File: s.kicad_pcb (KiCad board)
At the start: 2 copper layers, 3 parts, among them J1 USB4085-GF-A_REVB, U1 ESP32-S3-WROOM-1, U2 MCP1825S

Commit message: add supporting stuff and assigned footprints
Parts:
- added C1: 1uF, Capacitor_SMD:C_0805_2012Metric_Pad1.18x1.45mm_HandSolder, F.Cu at (187.0, 114.8)
- added C2: 10uF, Capacitor_SMD:C_0805_2012Metric_Pad1.18x1.45mm_HandSolder, F.Cu at (187.0, 117.8)
- added C3: 1uF, Capacitor_SMD:C_0805_2012Metric_Pad1.18x1.45mm_HandSolder, F.Cu at (187.0, 120.8)
- added C4: 0.1uF, Capacitor_SMD:C_0805_2012Metric_Pad1.18x1.45mm_HandSolder, F.Cu at (187.0, 123.8)
- added C5: 0.1uF, Capacitor_SMD:C_0805_2012Metric_Pad1.18x1.45mm_HandSolder, F.Cu at (187.0, 126.8)
- added C6: 10uF, Capacitor_SMD:C_0805_2012Metric_Pad1.18x1.45mm_HandSolder, F.Cu at (187.0, 129.8)
- added D1: ~, Diode_SMD:D_SOD-323_HandSoldering, F.Cu at (243.7, 42.4)
- added D10: ~, Diode_SMD:D_SOD-323_HandSoldering, F.Cu at (248.8, 48.3)
- added D11: ~, Diode_SMD:D_SOD-323_HandSoldering, F.Cu at (248.8, 51.2)
- added D12: ~, Diode_SMD:D_SOD-323_HandSoldering, F.Cu at (248.8, 54.2)
- added D13: ~, Diode_SMD:D_SOD-323_HandSoldering, F.Cu at (248.8, 57.1)
- added D14: ~, Diode_SMD:D_SOD-323_HandSoldering, F.Cu at (248.8, 60.1)
- added D15: ~, Diode_SMD:D_SOD-323_HandSoldering, F.Cu at (253.8, 42.4)
- added D16: ~, Diode_SMD:D_SOD-323_HandSoldering, F.Cu at (253.8, 45.3)
- added D17: ~, Diode_SMD:D_SOD-323_HandSoldering, F.Cu at (253.8, 48.3)
- added D18: ~, Diode_SMD:D_SOD-323_HandSoldering, F.Cu at (253.8, 51.2)
- added D19: ~, Diode_SMD:D_SOD-323_HandSoldering, F.Cu at (253.8, 54.2)
- added D2: ~, Diode_SMD:D_SOD-323_HandSoldering, F.Cu at (243.7, 45.3)
- added D20: ~, Diode_SMD:D_SOD-323_HandSoldering, F.Cu at (253.8, 57.1)
- added D21: ~, Diode_SMD:D_SOD-323_HandSoldering, F.Cu at (253.8, 60.1)
- added D22: ~, Diode_SMD:D_SOD-323_HandSoldering, F.Cu at (258.9, 42.4)
- added D23: ~, Diode_SMD:D_SOD-323_HandSoldering, F.Cu at (258.9, 45.3)
- added D24: ~, Diode_SMD:D_SOD-323_HandSoldering, F.Cu at (258.9, 48.3)
- added D25: ~, Diode_SMD:D_SOD-323_HandSoldering, F.Cu at (258.9, 51.2)
- added D26: ~, LED_SMD:LED_0805_2012Metric_Pad1.15x1.40mm_HandSolder, F.Cu at (176.4, 128.4)
- added D27: ~, LED_SMD:LED_0805_2012Metric_Pad1.15x1.40mm_HandSolder, F.Cu at (176.4, 131.4)
- added D28: ~, LED_SMD:LED_0805_2012Metric_Pad1.15x1.40mm_HandSolder, F.Cu at (176.4, 134.5)
- added D29: ~, LED_SMD:LED_0805_2012Metric_Pad1.15x1.40mm_HandSolder, F.Cu at (176.4, 137.5)
- added D3: ~, Diode_SMD:D_SOD-323_HandSoldering, F.Cu at (243.7, 48.3)
- added D4: ~, Diode_SMD:D_SOD-323_HandSoldering, F.Cu at (243.7, 51.2)
- added D5: ~, Diode_SMD:D_SOD-323_HandSoldering, F.Cu at (243.7, 54.2)
- added D6: ~, Diode_SMD:D_SOD-323_HandSoldering, F.Cu at (243.7, 57.1)
- added D7: ~, Diode_SMD:D_SOD-323_HandSoldering, F.Cu at (243.7, 60.1)
- added D8: ~, Diode_SMD:D_SOD-323_HandSoldering, F.Cu at (248.8, 42.4)
- added D9: ~, Diode_SMD:D_SOD-323_HandSoldering, F.Cu at (248.8, 45.3)
- added J2: UART connector, Connector_PinHeader_2.54mm:PinHeader_1x04_P2.54mm_Vertical, F.Cu at (181.1, 129.2)
- added R1: 10k, Resistor_SMD:R_0805_2012Metric_Pad1.20x1.40mm_HandSolder, F.Cu at (191.8, 114.8)
- added R2: 10k, Resistor_SMD:R_0805_2012Metric_Pad1.20x1.40mm_HandSolder, F.Cu at (191.8, 117.7)
- added R3: 100, Resistor_SMD:R_0805_2012Metric_Pad1.20x1.40mm_HandSolder, F.Cu at (191.8, 120.7)
- added R4: 100, Resistor_SMD:R_0805_2012Metric_Pad1.20x1.40mm_HandSolder, F.Cu at (191.8, 123.6)
- added R5: 100, Resistor_SMD:R_0805_2012Metric_Pad1.20x1.40mm_HandSolder, F.Cu at (191.8, 126.6)
- added R6: 100, Resistor_SMD:R_0805_2012Metric_Pad1.20x1.40mm_HandSolder, F.Cu at (191.8, 129.5)
- added SW1: Z, MX_Hotswap:MX-Hotswap-1U, F.Cu at (181.7, 48.4)
- added SW10: D, MX_Hotswap:MX-Hotswap-1U, F.Cu at (198.5, 68.6)
- added SW11: S, MX_Hotswap:MX-Hotswap-1U, F.Cu at (198.5, 78.6)
- added SW12: K, MX_Hotswap:MX-Hotswap-1U, F.Cu at (198.5, 88.7)
- added SW13: W, MX_Hotswap:MX-Hotswap-1U, F.Cu at (198.5, 98.7)
- added SW14: R, MX_Hotswap:MX-Hotswap-1U, F.Cu at (198.5, 108.8)
- added SW15: STAR, MX_Hotswap:MX-Hotswap-1U, F.Cu at (215.3, 48.4)
- added SW16: R, MX_Hotswap:MX-Hotswap-1U, F.Cu at (215.3, 58.5)
- added SW17: B, MX_Hotswap:MX-Hotswap-1U, F.Cu at (215.3, 68.6)
- added SW18: G, MX_Hotswap:MX-Hotswap-1U, F.Cu at (215.3, 78.6)
- added SW19: S, MX_Hotswap:MX-Hotswap-1U, F.Cu at (215.3, 88.7)
- added SW2: T, MX_Hotswap:MX-Hotswap-1U, F.Cu at (181.7, 58.5)
- added SW20: Z, MX_Hotswap:MX-Hotswap-1U, F.Cu at (215.3, 98.7)
- added SW21: A, MX_Hotswap:MX-Hotswap-1U, F.Cu at (215.3, 108.8)
- added SW22: O, MX_Hotswap:MX-Hotswap-1U, F.Cu at (232.1, 48.4)
- added SW23: NUM, MX_Hotswap:MX-Hotswap-1U, F.Cu at (232.1, 58.5)
- added SW24: E, MX_Hotswap:MX-Hotswap-1U, F.Cu at (232.1, 68.6)
- added SW25: U, MX_Hotswap:MX-Hotswap-1U, F.Cu at (232.1, 78.6)
- added SW26: 210-4MS, dip_switch_footprints:DIP8_210-4_CTS, F.Cu at (175.5, 116.3)
- added SW3: P, MX_Hotswap:MX-Hotswap-1U, F.Cu at (181.7, 68.6)
- added SW4: H, MX_Hotswap:MX-Hotswap-1U, F.Cu at (181.7, 78.6)
- added SW5: STAR, MX_Hotswap:MX-Hotswap-1U, F.Cu at (181.7, 88.7)
- added SW6: F, MX_Hotswap:MX-Hotswap-1U, F.Cu at (164.5, 99.5)
- added SW7: P, MX_Hotswap:MX-Hotswap-1U, F.Cu at (145.9, 99.5)
- added SW8: L, MX_Hotswap:MX-Hotswap-1U, F.Cu at (198.5, 48.4)
- added SW9: T, MX_Hotswap:MX-Hotswap-1U, F.Cu at (198.5, 58.5)
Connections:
- U1 pad 10: unconnected-(U1-IO17-Pad10) -> /led_2
- U1 pad 11: unconnected-(U1-IO18-Pad11) -> /led_3
- U1 pad 12: unconnected-(U1-IO8-Pad12) -> /matrix_c8
- U1 pad 15: unconnected-(U1-IO3-Pad15) -> /matrix_c3
- U1 pad 17: unconnected-(U1-IO9-Pad17) -> /matrix_c9
- U1 pad 18: unconnected-(U1-IO10-Pad18) -> /matrix_c10
- U1 pad 19: unconnected-(U1-IO11-Pad19) -> /matrix_r1
- U1 pad 20: unconnected-(U1-IO12-Pad20) -> /matrix_r2
- U1 pad 21: unconnected-(U1-IO13-Pad21) -> /matrix_r3
- U1 pad 22: unconnected-(U1-IO14-Pad22) -> /led_1
- U1 pad 23: unconnected-(U1-IO21-Pad23) -> /led_4
- U1 pad 27: unconnected-(U1-IO0-Pad27) -> Net-(U1-IO0)
- U1 pad 33: unconnected-(U1-IO40-Pad33) -> /sw_2
- U1 pad 34: unconnected-(U1-IO41-Pad34) -> /sw_3
- U1 pad 35: unconnected-(U1-IO42-Pad35) -> /sw_4
- U1 pad 36: unconnected-(U1-RXD0-Pad36) -> Net-(J2-Pin_3)
- U1 pad 37: unconnected-(U1-TXD0-Pad37) -> Net-(J2-Pin_2)
- U1 pad 38: unconnected-(U1-IO2-Pad38) -> /matrix_c2
- U1 pad 39: unconnected-(U1-IO1-Pad39) -> /matrix_c1
- U1 pad 4: unconnected-(U1-IO4-Pad4) -> /matrix_c4
- U1 pad 5: unconnected-(U1-IO5-Pad5) -> /matrix_c5
- U1 pad 6: unconnected-(U1-IO6-Pad6) -> /matrix_c6
- U1 pad 7: unconnected-(U1-IO7-Pad7) -> /matrix_c7

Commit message: update footprints
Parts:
- added C10: 10uF, Capacitor_SMD:C_0805_2012Metric_Pad1.18x1.45mm_HandSolder, F.Cu at (239.4, 111.8)
- added C11: 0.1uF, Capacitor_SMD:C_0805_2012Metric_Pad1.18x1.45mm_HandSolder, F.Cu at (239.4, 114.8)
- added C12: 4.7uF, Capacitor_SMD:C_0805_2012Metric_Pad1.18x1.45mm_HandSolder, F.Cu at (239.4, 117.8)
- added C7: 0.1uF, Capacitor_SMD:C_0805_2012Metric_Pad1.18x1.45mm_HandSolder, F.Cu at (239.4, 102.8)
- added C8: 10uF, Capacitor_SMD:C_0805_2012Metric_Pad1.18x1.45mm_HandSolder, F.Cu at (239.4, 105.8)
- added C9: 0.1uF, Capacitor_SMD:C_0805_2012Metric_Pad1.18x1.45mm_HandSolder, F.Cu at (239.4, 108.8)
- added D30: CHRG_STAT_LED, LED_SMD:LED_0805_2012Metric_Pad1.15x1.40mm_HandSolder, F.Cu at (239.4, 120.8)
- added J3: SW_PWR, Connector_PinHeader_2.54mm:PinHeader_1x03_P2.54mm_Vertical, F.Cu at (254.0, 118.4)
- added J4: Conn_01x02_Pin, Connector_JST:JST_PH_B2B-PH-K_1x02_P2.00mm_Vertical, F.Cu at (249.5, 112.3)
- added R10: 150, Resistor_SMD:R_0805_2012Metric_Pad1.20x1.40mm_HandSolder, F.Cu at (244.2, 119.9)
- added R7: 330, Resistor_SMD:R_0805_2012Metric_Pad1.20x1.40mm_HandSolder, F.Cu at (244.2, 111.0)
- added R8: 2k7, Resistor_SMD:R_0805_2012Metric_Pad1.20x1.40mm_HandSolder, F.Cu at (244.2, 114.0)
- added R9: 10k/2k, Resistor_SMD:R_0805_2012Metric_Pad1.20x1.40mm_HandSolder, F.Cu at (244.2, 117.0)
- added U3: MCP1825S, Package_TO_SOT_SMD:SOT-223-3_TabPin2, F.Cu at (246.7, 105.5)
- added U4: AP9101CK, Package_TO_SOT_SMD:SOT-23-5, F.Cu at (249.1, 118.5)
- added U5: MCP73831-2-OT, Package_TO_SOT_SMD:SOT-23-5, F.Cu at (249.1, 123.2)
- added U6: DMG6968U-7, DMG6968U_7:SOT95P240X110-3N, F.Cu at (253.8, 103.3)
- added U7: DMG6968U-7, DMG6968U_7:SOT95P240X110-3N, F.Cu at (253.8, 107.5)

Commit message: move stuff around on pcb
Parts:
- D1, D10, D11, D12, D13, D14, D15, D16, D17, D18, D19, D2, D20, D21, D22, D23, D24, D25, D3, D4, D5, D6, D7, D8, D9, J1, SW1, SW10, SW11, SW12, SW13, SW14, SW15, SW16, SW17, SW18, SW19, SW2, SW20, SW21, SW22, SW23, SW24, SW25, SW3, SW4, SW5, SW6, SW7, SW8, SW9, U1: moved to B.Cu
- moved J3 200.2 mm to (53.8, 120.7), turned to 90 degrees
- moved D11 196.4 mm to (57.9, 97.6), turned to 90 degrees
- moved J4 193.4 mm to (56.1, 113.3), turned to -90 degrees
- moved D1 189.2 mm to (57.9, 78.6), turned to 90 degrees
- moved U4 187.2 mm to (62.2, 128.5)
- moved U5 187.2 mm to (62.2, 133.2)
- moved U6 187.2 mm to (66.9, 113.3)
- moved U7 187.2 mm to (66.9, 117.5)
- moved D12 177.2 mm to (77.0, 97.6), turned to 90 degrees
- moved R10 171.7 mm to (72.4, 120.0)
- moved R7 171.7 mm to (72.4, 111.1)
- moved R8 171.7 mm to (72.4, 114.1)
- moved R9 171.7 mm to (72.4, 117.0)
- moved D2 170.0 mm to (77.0, 78.6), turned to 90 degrees
- moved D30 169.8 mm to (69.8, 130.2)
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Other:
- board outline added: 200 x 75 mm

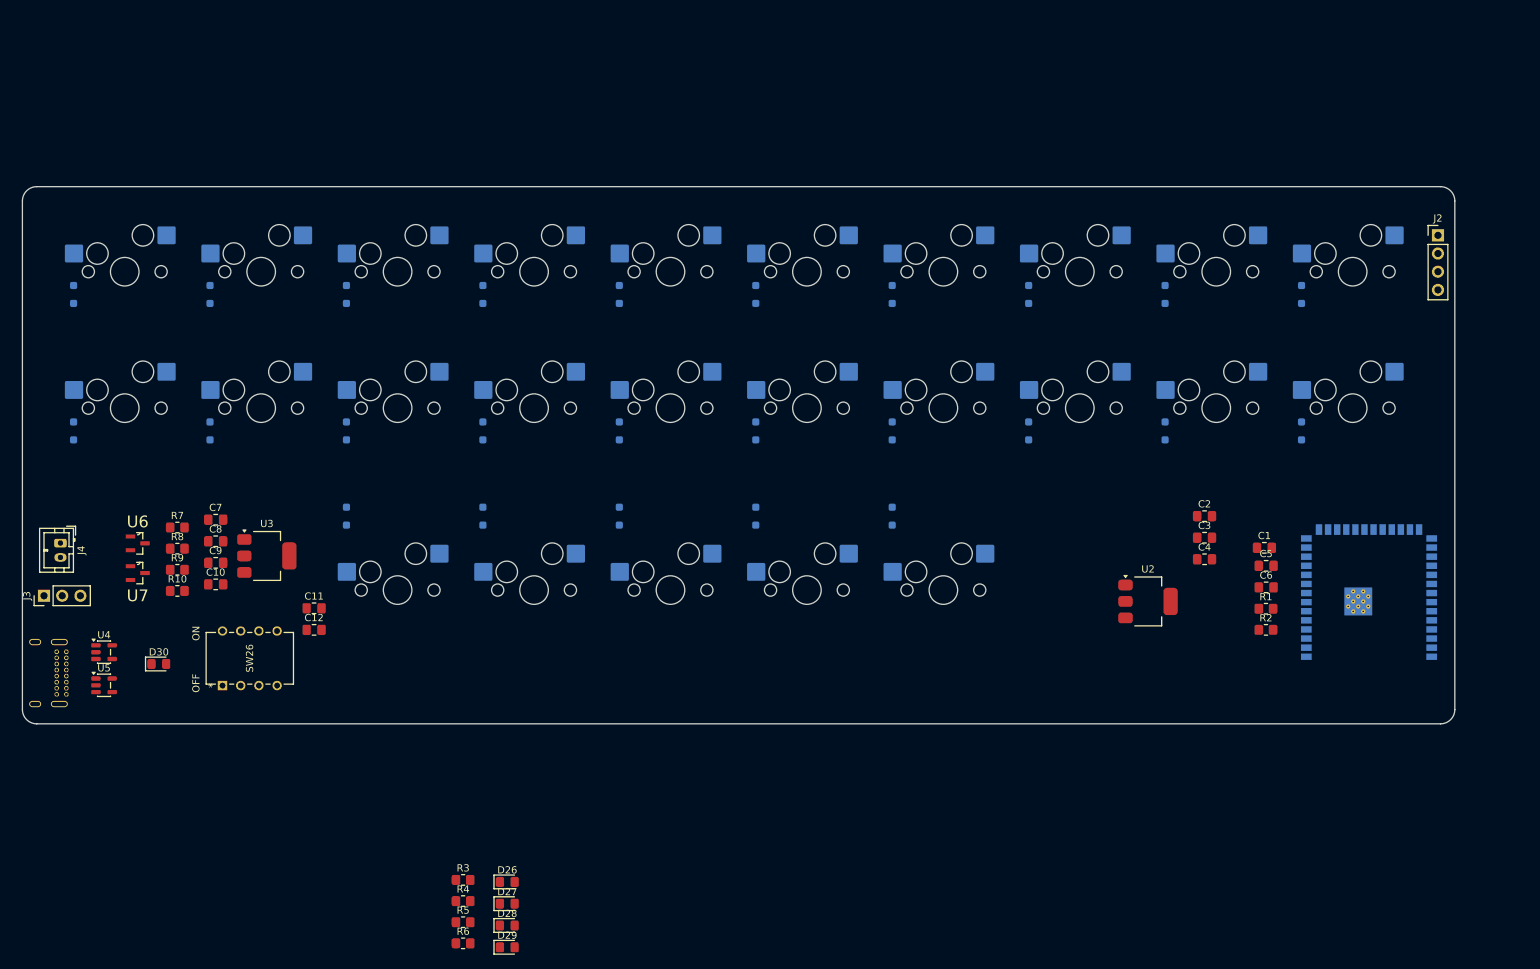
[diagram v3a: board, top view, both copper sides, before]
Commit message: routed the key matrix
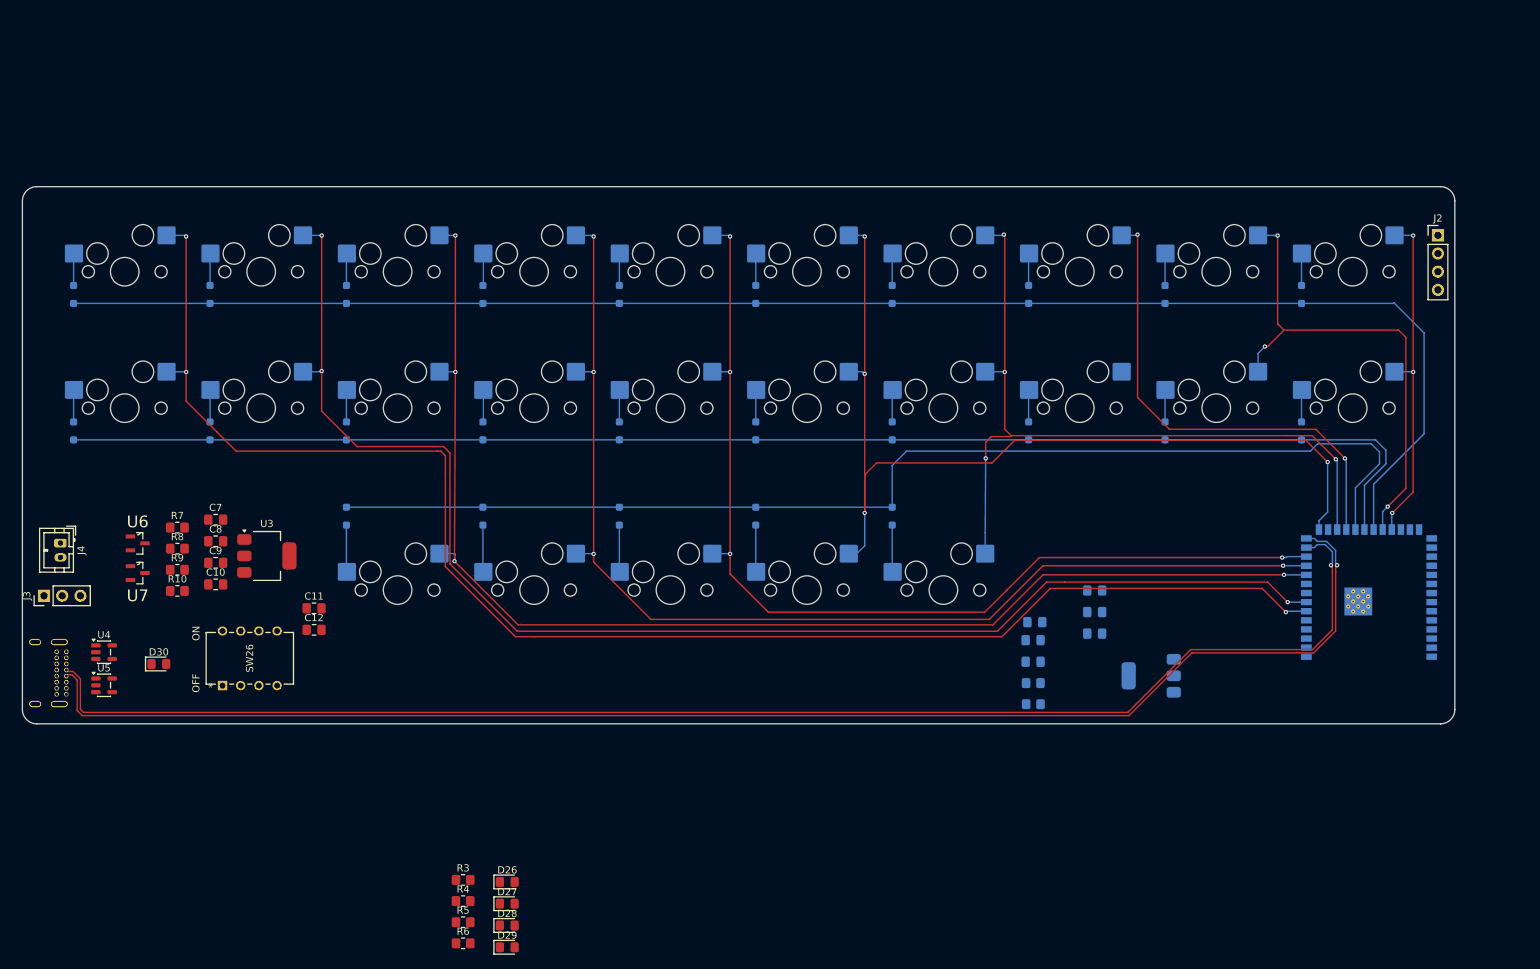
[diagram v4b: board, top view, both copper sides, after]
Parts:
- C1, C2, C3, C4, C5, C6, R1, R2, U2: moved to B.Cu
- moved C5 34.2 mm to (191.9, 126.9), turned to 180 degrees
- moved C6 34.2 mm to (191.9, 129.9), turned to 180 degrees
- moved R1 34.1 mm to (191.9, 132.8), turned to 180 degrees
- moved R2 34.1 mm to (191.9, 135.8), turned to 180 degrees
- moved C1 33.7 mm to (192.2, 124.3), turned to 180 degrees
- moved C2 18.5 mm to (200.5, 119.9), turned to 180 degrees
- moved C3 18.5 mm to (200.5, 122.9), turned to 180 degrees
- moved C4 18.5 mm to (200.5, 125.9), turned to 180 degrees
- moved U2 10.4 mm to (208.4, 131.8), turned to 180 degrees
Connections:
- U1 pad 10: /led_2 -> /matrix_c3
- U1 pad 11: /led_3 -> /matrix_c4
- U1 pad 12: /matrix_c8 -> /matrix_c5
- U1 pad 15: /matrix_c3 -> /matrix_c6
- U1 pad 17: /matrix_c9 -> /matrix_c7
- U1 pad 18: /matrix_c10 -> /matrix_c8
- U1 pad 19: /matrix_r1 -> /matrix_r3
- U1 pad 21: /matrix_r3 -> /matrix_r1
- U1 pad 22: /led_1 -> /matrix_c9
- U1 pad 23: /led_4 -> /matrix_c10
- U1 pad 38: /matrix_c2 -> /led_1
- U1 pad 39: /matrix_c1 -> /led_2
- U1 pad 4: /matrix_c4 -> /led_3
- U1 pad 5: /matrix_c5 -> /led_4
- U1 pad 6: /matrix_c6 -> /matrix_c1
- U1 pad 7: /matrix_c7 -> /matrix_c2
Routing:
- net /matrix_r1: track 0.00 -> 220.7 mm
- net /matrix_c1: track 0.00 -> 211.8 mm, vias 0 -> 3
- net /USB_D+: track 0.00 -> 203.2 mm, vias 0 -> 1
- net /USB_D-: track 0.00 -> 201.8 mm, vias 0 -> 1
- net /matrix_r2: track 0.00 -> 196.1 mm
- net /matrix_c2: track 0.00 -> 193.3 mm, vias 0 -> 3
- net /matrix_c3: track 0.00 -> 178.7 mm, vias 0 -> 4
- net /matrix_r3: track 0.00 -> 164.0 mm
- net /matrix_c4: track 0.00 -> 158.9 mm, vias 0 -> 4
- net /matrix_c5: track 0.00 -> 140.5 mm, vias 0 -> 4
- net /matrix_c6: track 0.00 -> 133.7 mm, vias 0 -> 4
- net /matrix_c7: track 0.00 -> 110.0 mm, vias 0 -> 4
- net /matrix_c9: track 0.00 -> 69.5 mm, vias 0 -> 3
- net /matrix_c8: track 0.00 -> 67.5 mm, vias 0 -> 2
- net /matrix_c10: track 0.00 -> 47.5 mm, vias 0 -> 3
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
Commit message: quick commit: moved stuff around and deleted a capacitor
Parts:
- removed C3: 1uF, Capacitor_SMD:C_0805_2012Metric_Pad1.18x1.45mm_HandSolder
- C4: moved to F.Cu
- moved R2 117.3 mm to (75.2, 124.6)
- moved C6 35.0 mm to (226.9, 128.2), turned to -90 degrees
- moved C5 32.0 mm to (223.9, 128.2), turned to -90 degrees
- moved R1 30.4 mm to (221.5, 125.8), turned to 90 degrees
- moved C1 29.4 mm to (221.5, 121.9), turned to 90 degrees
- moved C4 0.73 mm to (200.6, 125.2)

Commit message: route some more stuff
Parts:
- C4: moved to B.Cu
- moved C4 18.5 mm to (218.4, 120.3), turned to 90 degrees
- moved C2 14.4 mm to (214.9, 120.3), turned to 90 degrees
- moved U2 8.27 mm to (214.5, 126.2)
- moved R1 0.40 mm to (221.2, 126.1)
- moved C1 0.25 mm to (221.2, 121.9)
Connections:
- net Net-(J2-Pin_2) renamed /UART_TX
- net Net-(J2-Pin_3) renamed /UART_RX
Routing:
- net /CC2: track 0.00 -> 202.1 mm, vias 0 -> 1
- net /CC1: track 0.00 -> 192.5 mm, vias 0 -> 1
- net /VBUS: track 0.00 -> 190.5 mm
- net +3.3V: track 0.00 -> 87.7 mm, vias 0 -> 1
- net /UART_TX: track 0.00 -> 57.2 mm, vias 0 -> 1
- net /UART_RX: track 0.00 -> 52.4 mm, vias 0 -> 1
- net GND: track 0.00 -> 18.8 mm
- net Net-(U1-EN): track 0.00 -> 12.6 mm
- net /matrix_c9: track 69.5 -> 59.2 mm
- net /matrix_c10: track 47.5 -> 46.0 mm
- net /USB_D-: track 201.8 -> 203.0 mm
- net /USB_D+: track 203.2 -> 204.5 mm
